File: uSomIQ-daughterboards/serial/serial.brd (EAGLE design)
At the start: 100 x 80 mm, 1 part

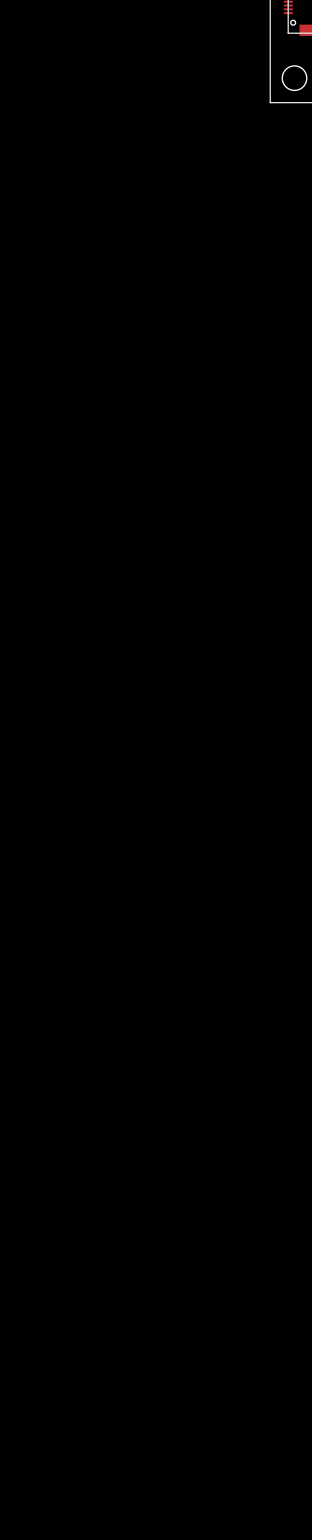
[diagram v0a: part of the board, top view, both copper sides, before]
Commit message: Add power supply and RTC
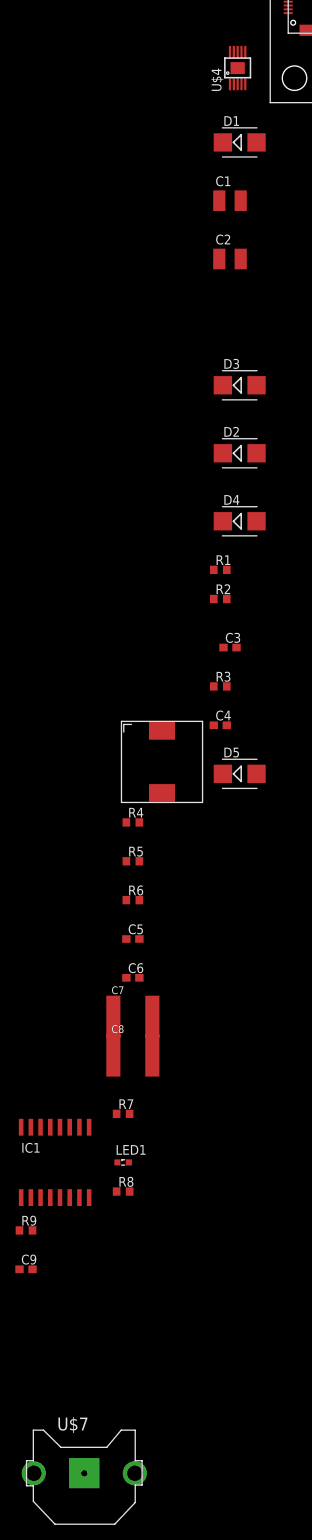
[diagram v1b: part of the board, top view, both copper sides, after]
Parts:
- added C1, C2: 4.7uF, 50V, rcl:C1210
- added C3: 0.01uF, 50V, rcl:C0603
- added C4: 0.1uF, 50V, rcl:C0603
- added C5: 5600pF, 25V, rcl:C0603
- added C6: 330pF, 50V, rcl:C0603
- added C7, C8: 47uF, 16V, rcl:C2220K
- added C9: 1uF, 16V, rcl:C0603
- added D1, D2, D5: B360B, diode:SMB
- added D3, D4: 47V, diode:SMB
- added IC1: DS3231/SO, adafruit:SO16W
- added L1: 27uH, 4.3A, power-supplies:7447798271
- added LED1: (no value), led:SML0603
- added R1: 384K, rcl:R0603
- added R2: 69.8K, rcl:R0603
- added R3: 412K, rcl:R0603
- added R4: 53.6K, rcl:R0603
- added R5, R7: 10K, rcl:R0603
- added R6: 11K, rcl:R0603
- added R8, R9: 100, rcl:R0603
- added U$4: TPS54260, power-supplies:S-PDSO-G10
- added U$7: (no value), adafruit:CR1220-THM
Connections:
- new net GND: C1.2, C2.2, C3.2, C5.2, C6.2, C7.2, C8.2, C9.2, D3.A, D4.A, D5.A, IC1.13, LED1.C, R2.1, R3.1, R5.1, U$3.MOUNT@0, U$3.MOUNT@1, U$3.MOUNT@2, U$3.MOUNT@3, U$4.9, U$4.PAD, U$7.-
- new net I2C0_SCL: IC1.16
- new net I2C0_SDA: IC1.15
- new net N$1: C1.1, C2.1, D1.C, D3.C, U$4.2
- new net N$10: C6.1, R6.2, U$4.8
- new net N$11: C5.1, R6.1
- new net N$12: IC1.14, U$7.+1
- new net N$2: C3.1, U$4.4
- new net N$3: D2.C, D4.C, R1.1
- new net N$4: R1.2, R2.2, U$4.3
- new net N$5: R3.2, U$4.5
- new net N$6: C4.1, U$4.1
- new net N$7: C4.2, D5.C, L1.P$1, U$4.10
- new net N$8: IC1.1, R9.2
- new net N$9: R4.1, R5.2, U$4.7
- new net RESET: R8.1
- new net RTC_32KHZ: R9.1
- new net VBATT: D1.A
- new net VDD: C7.1, C8.1, C9.1, IC1.2, L1.P$2, R4.2, R7.2
- new net VDD_PGOOD: LED1.A, R7.1, R8.2, U$4.6
- new net VIGN: D2.A

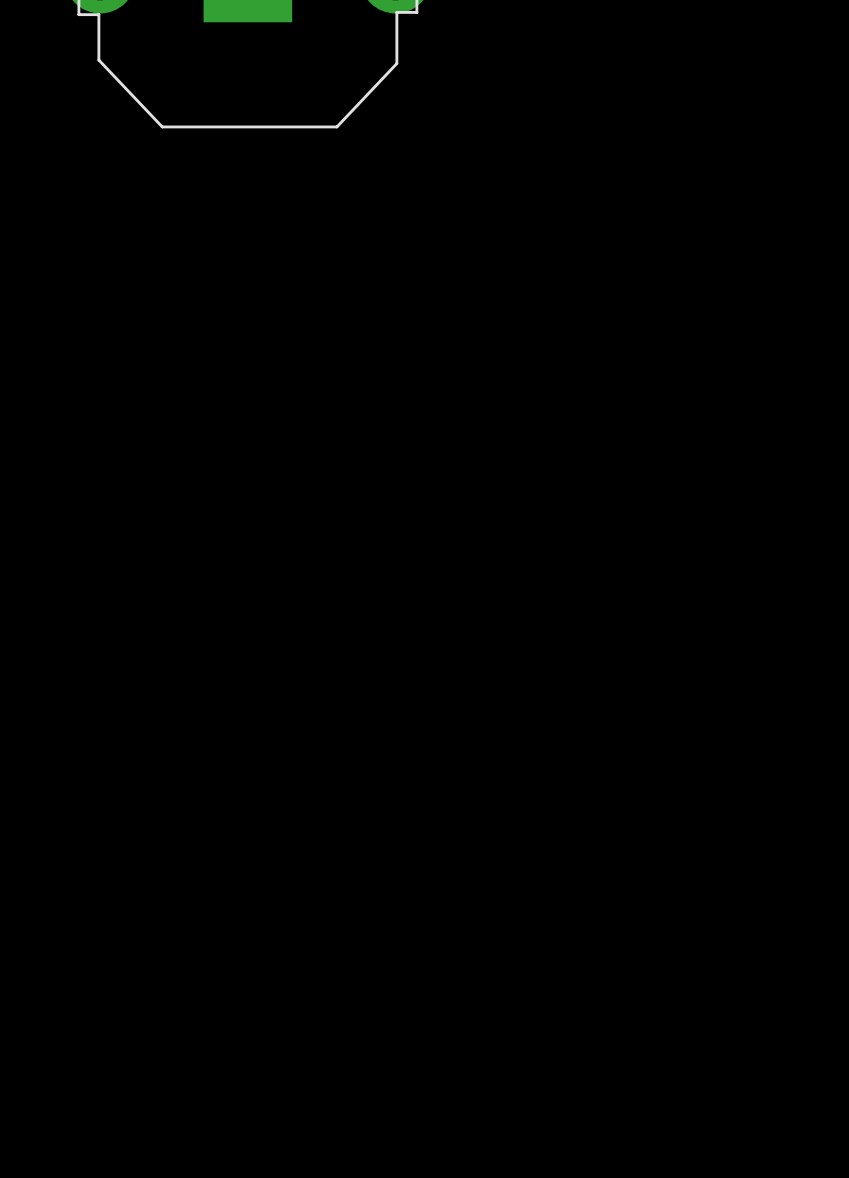
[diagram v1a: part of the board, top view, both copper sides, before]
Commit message: Add serial port connectors
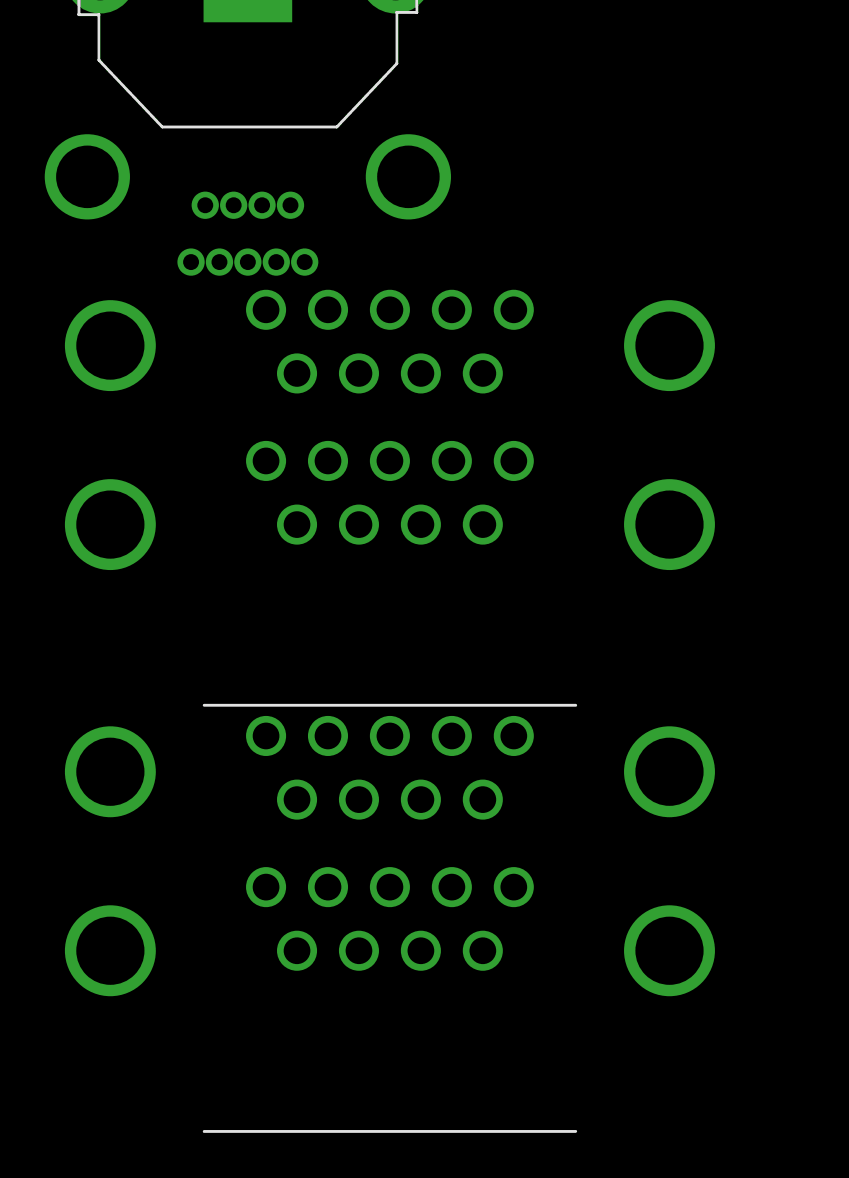
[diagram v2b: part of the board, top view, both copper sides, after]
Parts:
- added U$6: 83611-9006, connectors:83611-9006
- added U$8, U$9: 189-009-613R571, connectors:189-009-613R571
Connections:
- new net CAN_H: U$6.5
- new net CAN_L: U$6.6
- new net ETH_RX+: U$6.3
- new net ETH_RX-: U$6.4
- new net ETH_TX+: U$6.1
- new net ETH_TX-: U$6.2
- new net SP0-1PPS: U$8.A-1
- new net SP0-RX: U$8.A-2
- new net SP0-TX: U$8.A-3
- new net SP1-1PPS: U$8.B-1
- new net SP1-RX: U$8.B-3
- new net SP1-TX: U$8.B-4
- new net SP2-1PPS: U$9.A-1
- new net SP2-RX: U$9.A-2
- new net SP2-TX: U$9.A-3
- new net SP3-1PPS: U$9.B-1
- new net SP3-RX: U$9.B-3
- new net SP3-TX: U$9.B-4
- net GND: now also U$6.9, U$6.MOUNT@1, U$6.MOUNT@2, U$8.A-5, U$8.B2, U$8.MOUNT@1, U$8.MOUNT@2, U$8.MOUNT@3, U$8.MOUNT@4, U$9.A-5, U$9.B2, U$9.MOUNT@1, U$9.MOUNT@2, U$9.MOUNT@3, U$9.MOUNT@4
- net VBATT: now also U$6.7
- net VIGN: now also U$6.8
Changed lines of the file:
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@@
 <element name="C9" library="rcl" package="C0603" value="1uF, 16V" x="-100.33" y="-152.4"/>
 <element name="U$7" library="adafruit" package="CR1220-THM" value="" x="-92.71" y="-179.07"/>
+<element name="U$6" library="connectors" package="83611-9006" value="83611-9006" x="-95.25" y="-191.77"/>
+<element name="U$8" library="connectors" package="189-009-613R571" value="189-009-613R571" x="-86.36" y="-200.66"/>
+<element name="U$9" library="connectors" package="189-009-613R571" value="189-009-613R571" x="-86.36" y="-219.71"/>
 </elements>
 <signals>
 <signal name="VBATT">
 <contactref element="D1" pad="A"/>
+<contactref element="U$6" pad="7"/>
+<wire x1="-93.345" y1="-189.23" x2="-70.19" y2="-5.08" width="0" layer="19" extent="1-1"/>
 </signal>
 <signal name="N$1">
@@
 <contactref element="C9" pad="2"/>
 <contactref element="U$7" pad="-"/>
+<contactref element="U$6" pad="9"/>
+<contactref element="U$6" pad="MOUNT@1"/>
+<contactref element="U$6" pad="MOUNT@2"/>
+<contactref element="U$8" pad="MOUNT@1"/>
+<contactref element="U$8" pad="MOUNT@2"/>
+<contactref element="U$8" pad="MOUNT@3"/>
+<contactref element="U$8" pad="MOUNT@4"/>
+<contactref element="U$9" pad="MOUNT@1"/>
+<contactref element="U$9" pad="MOUNT@2"/>
+<contactref element="U$9" pad="MOUNT@3"/>
+<contactref element="U$9" pad="MOUNT@4"/>
+<contactref element="U$8" pad="A-5"/>
+<contactref element="U$8" pad="B2"/>
+<contactref element="U$9" pad="A-5"/>
+<contactref element="U$9" pad="B2"/>
 <wire x1="-88.38" y1="-138.43" x2="-99.48" y2="-152.4" width="0" layer="19" extent="1-1"/>
 <wire x1="-97.155" y1="-133.83" x2="-88.38" y2="-138.43" width="0" layer="19" extent="1-1"/>
@@
 <wire x1="-63.5" y1="31.0575" x2="-63.5" y2="9.5825" width="0" layer="19" extent="1-1"/>
 <wire x1="-92.71" y1="-179.07" x2="-99.48" y2="-152.4" width="0" layer="19" extent="1-1"/>
+<wire x1="-90.805" y1="-189.23" x2="-92.71" y2="-179.07" width="0" layer="19" extent="1-1"/>
+<wire x1="-89.1286" y1="-193.9036" x2="-90.805" y2="-189.23" width="0" layer="19" extent="1-1"/>
+<wire x1="-85.5345" y1="-187.96" x2="-90.805" y2="-189.23" width="0" layer="19" extent="1-1"/>
+<wire x1="-99.8855" y1="-187.96" x2="-90.805" y2="-189.23" width="0" layer="19" extent="1-1"/>
+<wire x1="-98.8568" y1="-195.5038" x2="-99.8855" y2="-187.96" width="0" layer="19" extent="1-1"/>
+<wire x1="-98.8568" y1="-203.5048" x2="-98.8568" y2="-195.5038" width="0" layer="19" extent="1-1"/>
+<wire x1="-80.8228" y1="-200.66" x2="-89.1286" y2="-193.9036" width="0" layer="19" extent="1-1"/>
+<wire x1="-73.8632" y1="-203.5048" x2="-80.8228" y2="-200.66" width="0" layer="19" extent="1-1"/>
+<wire x1="-73.8632" y1="-195.5038" x2="-73.8632" y2="-203.5048" width="0" layer="19" extent="1-1"/>
+<wire x1="-98.8568" y1="-214.5538" x2="-98.8568" y2="-203.5048" width="0" layer="19" extent="1-1"/>
+<wire x1="-98.8568" y1="-222.5548" x2="-98.8568" y2="-214.5538" width="0" layer="19" extent="1-1"/>
+<wire x1="-89.1286" y1="-212.9536" x2="-98.8568" y2="-214.5538" width="0" layer="19" extent="1-1"/>
+<wire x1="-80.8228" y1="-219.71" x2="-89.1286" y2="-212.9536" width="0" layer="19" extent="1-1"/>
+<wire x1="-73.8632" y1="-222.5548" x2="-80.8228" y2="-219.71" width="0" layer="19" extent="1-1"/>
+<wire x1="-73.8632" y1="-214.5538" x2="-73.8632" y2="-222.5548" width="0" layer="19" extent="1-1"/>
 <wire x1="-17.5" y1="31.0575" x2="-63.5" y2="31.0575" width="0" layer="19" extent="1-1"/>
 <wire x1="-17.5" y1="9.5825" x2="-17.5" y2="31.0575" width="0" layer="19" extent="1-1"/>
@@
 <signal name="VIGN">
 <contactref element="D2" pad="A"/>
+<contactref element="U$6" pad="8"/>
+<wire x1="-92.075" y1="-189.23" x2="-70.19" y2="-45.72" width="0" layer="19" extent="1-1"/>
 </signal>
 <signal name="N$3">
@@
 <wire x1="-99.314" y1="-179.07" x2="-98.425" y2="-133.83" width="0" layer="19" extent="1-1"/>
 </signal>
+<signal name="ETH_TX+">
+<contactref element="U$6" pad="1"/>
+</signal>
+<signal name="ETH_TX-">
+<contactref element="U$6" pad="2"/>
+</signal>
+<signal name="ETH_RX+">
+<contactref element="U$6" pad="3"/>
+</signal>
+<signal name="ETH_RX-">
+<contactref element="U$6" pad="4"/>
+</signal>
+<signal name="CAN_H">
+<contactref element="U$6" pad="5"/>
+</signal>
+<signal name="CAN_L">
+<contactref element="U$6" pad="6"/>
+</signal>
+<signal name="SP0-RX">
+<contactref element="U$8" pad="A-2"/>
+</signal>
+<signal name="SP0-TX">
+<contactref element="U$8" pad="A-3"/>
+</signal>
+<signal name="SP1-RX">
+<contactref element="U$8" pad="B-3"/>
+</signal>
+<signal name="SP1-TX">
+<contactref element="U$8" pad="B-4"/>
+</signal>
+<signal name="SP2-RX">
+<contactref element="U$9" pad="A-2"/>
+</signal>
+<signal name="SP2-TX">
+<contactref element="U$9" pad="A-3"/>
+</signal>
+<signal name="SP3-RX">
+<contactref element="U$9" pad="B-3"/>
+</signal>
+<signal name="SP3-TX">
+<contactref element="U$9" pad="B-4"/>
+</signal>
+<signal name="SP0-1PPS">
+<contactref element="U$8" pad="A-1"/>
+</signal>
+<signal name="SP1-1PPS">
+<contactref element="U$8" pad="B-1"/>
+</signal>
+<signal name="SP2-1PPS">
+<contactref element="U$9" pad="A-1"/>
+</signal>
+<signal name="SP3-1PPS">
+<contactref element="U$9" pad="B-1"/>
+</signal>
 </signals>

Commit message: Add RS232 transcievers
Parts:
- added C10, C11, C12, C13, C14, C17, C18, C19, C20, C21: 0.1uF, resistor:C0603
- added C15, C16, C22, C23: 10uF, resistor:C0603
- added R10, R11, R12, R13, R14, R15, R16, R17: 1k, resistor:R0603
- added TP1, TP2, TP3, TP4: TPB1,27, testpad:B1,27
- added U$10, U$11: ADM3311E, misc-ics:TSSOP28
- moved U$6 279.5 mm to (67.3, 35.6), turned to 270 degrees
- moved U$8 267.0 mm to (10.2, 48.3), turned to 270 degrees
- moved U$9 256.4 mm to (10.2, 17.8), turned to 270 degrees
- moved U$7 238.3 mm to (31.8, 24.1), turned to 270 degrees
- moved IC1 220.6 mm to (30.5, 41.9)
- moved L1 186.9 mm to (54.6, 36.8)
- moved U$3 105.9 mm to (41.9, 10.2), turned to 90 degrees
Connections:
- new net +3V3: C10.2, C15.1, C16.1, C17.2, C22.1, C23.1, R16.2, R17.2, U$10.3, U$11.3, U$3.P$6, U$3.P$8
- new net +5V: C7.1, C8.1, L1.P$2, R4.2, U$3.P$2, U$3.P$4
- new net N$13: C10.1, U$10.1
- new net N$14: C17.1, U$11.1
- new net N$15: C11.1, U$10.2
- new net N$16: C11.2, U$10.4
- new net N$17: R10.2, U$10.9
- new net N$18: TP1.TP, U$10.14
- new net N$19: TP2.TP, U$10.20
- new net N$20: R11.2, U$10.15
- new net N$21: R12.2, U$10.23
- new net N$22: C12.1, U$10.6
- new net N$23: C12.2, U$10.24
- new net N$24: C13.2, U$10.25
- new net N$25: C18.1, U$11.2
- new net N$26: C14.2, U$10.26
- new net N$27: C14.1, U$10.28
- new net N$28: C18.2, U$11.4
- new net N$29: R13.2, U$11.9
- new net N$30: TP3.TP, U$11.14
- new net N$31: TP4.TP, U$11.20
- new net N$32: R14.2, U$11.15
- new net N$33: R15.2, U$11.23
- new net N$34: C19.1, U$11.6
- new net N$35: C19.2, U$11.24
- new net N$36: C20.2, U$11.25
- new net N$37: C21.2, U$11.26
- new net N$38: C21.1, U$11.28
- new net N$40: R7.2
- new net SP0_1PPS: U$10.18, U$11.18
- new net SP0_RX: U$10.19, U$11.19
- new net SP0_TX: U$10.22, U$11.22
- new net SP1_1PPS: U$10.16, U$11.16
- new net SP1_RX: U$10.17, U$11.17
- new net SP1_TX: U$10.21, U$11.21
- new net UART0_1PPS: U$10.11, U$11.11, U$3.P$33
- new net UART0_RX: U$10.10, U$11.10, U$3.P$29
- new net UART0_TX: U$10.7, U$11.7, U$3.P$31
- new net UART1_1PPS: U$10.13, U$11.13, U$3.P$40
- new net UART1_RX: U$10.12, U$11.12, U$3.P$37
- new net UART1_TX: U$10.8, U$11.8, U$3.P$39
- new net UART2_1PPS: U$3.P$50
- new net UART2_RX: U$3.P$49
- new net UART2_TX: U$3.P$47
- new net UART3_1PPS: U$3.P$46
- new net UART3_RX: U$3.P$41
- new net UART3_TX: U$3.P$43
- new net XCVR_EN: R16.1, R17.1, U$10.5, U$11.5
- net GND: now also C13.1, C15.2, C16.2, C20.1, C22.2, C23.2, R10.1, R11.1, R12.1, R13.1, R14.1, R15.1, U$10.27, U$11.27, U$3.P$1, U$3.P$3
- net I2C0_SCL: now also U$3.P$12
- net I2C0_SDA: now also U$3.P$10
- net VDD: no longer C7.1, C8.1, L1.P$2, R4.2, R7.2

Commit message: Update libraries, add power supply monitoring
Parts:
- added C201: 0.1uF, rcl:C1210
- added C210, C211: 0.1uF, rcl:C0603
- added D202, D207: BAS40, diode:SOT23
- added D208, D209: 1.8V, diode:SMB
- added LED301, LED302: (no value), led:SML0603
- added R209, R210: 20K, rcl:R0603
- added R211, R212: 1K, rcl:R0603
- added R301, R302: 10K, rcl:R0603
- added R405: 100, rcl:R0603
- added X301: MINI-USB-UX60-MB-5ST, con-hirose:UX60-MB-5ST
- R201: value 100 -> NL
- renumbered C1 to C202, C10 to C403, C11 to C402, C12 to C405, C13 to C407, C14 to C408, C15 to C401, C16 to C404, C17 to C411, C18 to C410, C19 to C413, C2 to C203, C20 to C414, C21 to C415, C22 to C409, C23 to C412, C3 to C204, C4 to C205, C5 to C206, C6 to C207, C7 to C208, C8 to C209, C9 to C406, D1 to D201, D2 to D203, D3 to D204, D4 to D205, D5 to D206, IC1 to IC401, L1 to L201, LED1 to LED201, R1 to R203, R10 to R402, R11 to R403, R12 to R406, R13 to R408, R14 to R409, R15 to R410, R16 to R401, R17 to R407, R2 to R204, R3 to R205, R4 to R207, R5 to R208, R6 to R206, R7 to R202, R8 to R201, R9 to R404, U$10 to U401, U$11 to U402, U$3 to P301, U$4 to U201, U$6 to P102, U$7 to B401, U$8 to P101, U$9 to P103
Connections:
- removed net N$1: C202.1, C203.1, D201.C, D204.C, U201.2
- removed net SP0-1PPS: P101.A-1
- removed net SP0-RX: P101.A-2
- removed net SP0-TX: P101.A-3
- removed net SP1-1PPS: P101.B-1
- removed net SP1-RX: P101.B-3
- removed net SP1-TX: P101.B-4
- removed net SP2-1PPS: P103.A-1
- removed net SP2-RX: P103.A-2
- removed net SP2-TX: P103.A-3
- removed net SP3-1PPS: P103.B-1
- removed net SP3-RX: P103.B-3
- removed net SP3-TX: P103.B-4
- removed net VDD: C406.1, IC401.2
- new net ADC_VBATT: C211.1, D209.C, P301.P$13, R210.2, R212.2
- new net ADC_VIGN: C210.1, D208.C, P301.P$11, R209.2, R211.2
- new net LED_ETH_100MB: P301.P$67, R301.2
- new net LED_ETH_ACTIVE: P301.P$69, R302.2
- new net N$39: IC401.4, R405.2
- new net N$42: D207.3, R209.1
- new net PWR_EN: D202.1, P301.P$38
- new net RTC_RST: R405.1
- new net SP2_1PPS: P103.A-1, U402.18
- new net SP2_RX: P103.A-2, U402.19
- new net SP2_TX: P103.A-3, U402.22
- new net SP3_1PPS: P103.B-1, U402.16
- new net SP3_RX: P103.B-3, U402.17
- new net SP3_TX: P103.B-4, U402.21
- new net USB_D+: P301.P$61, X301.3
- new net USB_D-: P301.P$63, X301.2
- new net VBATT_PROTECTED: C201.1, C202.1, C203.1, D201.C, D204.C, R210.1, U201.2
- new net VDD_PGOOD1: LED301.A, R301.1
- new net VDD_PGOOD2: LED302.A, R302.1
- net +3V3: now also C406.1, IC401.2
- net ETH_RX+: now also P301.P$62
- net ETH_RX-: now also P301.P$64, P301.P$70
- net ETH_TX+: now also P301.P$68
- net GND: now also C201.2, C210.2, C211.2, D208.A, D209.A, LED301.C, LED302.C, P301.P$129, P301.P$135, P301.P$27, P301.P$59, P301.P$60, P301.P$65, P301.P$66, P301.P$9, P301.P$91, P301.P$92, R211.1, R212.1, X301.5
- net SP0_1PPS: now also P101.A-1; no longer U402.18
- net SP0_RX: now also P101.A-2; no longer U402.19
- net SP0_TX: now also P101.A-3; no longer U402.22
- net SP1_1PPS: now also P101.B-1; no longer U402.16
- net SP1_RX: now also P101.B-3; no longer U402.17
- net SP1_TX: now also P101.B-4; no longer U402.21
- net UART0_1PPS: no longer U402.11
- net UART0_RX: no longer U402.10
- net UART0_TX: no longer U402.7
- net UART1_1PPS: no longer U402.13
- net UART1_RX: no longer U402.12
- net UART1_TX: no longer U402.8
- net UART2_1PPS: now also U402.11
- net UART2_RX: now also U402.10
- net UART2_TX: now also U402.7
- net UART3_1PPS: now also U402.13
- net UART3_RX: now also U402.12
- net UART3_TX: now also U402.8
- net VIGN: now also D207.1

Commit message: Start to place serial daughterboard power supply
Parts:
- removed C203: 4.7uF, 50V, rcl:C1210
- removed C208: 47uF, 16V, rcl:C2220K
- removed D203: B360B, diode:SMB
- removed R201: NL, rcl:R0603
- added D1: BAS40, diode:SOT23
- added TP5, TP6: TPB1,27, testpad:B1,27
- D205: device diode:SMB -> diode:SOT23
- moved X301 424.6 mm to (57.1, 26.7), turned to 180 degrees
- moved LED302 418.6 mm to (59.7, 15.2), turned to 180 degrees
- moved LED301 411.6 mm to (59.7, 17.8), turned to 180 degrees
- moved D207 411.5 mm to (16.5, 76.2), turned to 270 degrees
- moved R302 411.3 mm to (54.6, 15.2), turned to 180 degrees
- moved R301 404.3 mm to (54.6, 17.8), turned to 180 degrees
- moved C201 395.6 mm to (27.9, 63.5), turned to 270 degrees
- moved D202 366.7 mm to (16.5, 72.4), turned to 270 degrees
- moved U402 282.3 mm to (29.2, 20.3), turned to 90 degrees
- moved LED201 251.3 mm to (34.3, 81.3), turned to 180 degrees
- moved C209 242.4 mm to (45.7, 78.7), turned to 180 degrees
- moved U401 236.8 mm to (29.2, 41.9), turned to 90 degrees
- moved C207 221.2 mm to (34.3, 71.1), turned to 270 degrees
- moved C206 215.6 mm to (31.8, 71.1), turned to 90 degrees
- moved R206 209.9 mm to (29.2, 71.1), turned to 90 degrees
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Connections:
- removed net N$40: R202.2
- removed net RESET: R201.1
- removed net RTC_32KHZ: R404.1
- removed net RTC_RST: R405.1
- new net N$1: R404.1, TP5.TP
- new net N$41: R405.1, TP6.TP
- net +5V: now also R202.2; no longer C208.1
- net ETH_RX-: no longer P301.P$70
- net ETH_TX-: now also P301.P$70
- net GND: now also D205.1; no longer C203.2, C208.2, D205.A
- net N$3: now also D1.3, D205.3; no longer D203.C, D205.C
- net N$4: now also D202.3
- net VBATT_PROTECTED: no longer C203.1
- net VDD_PGOOD: no longer R201.2
- net VIGN: now also D1.1; no longer D203.A
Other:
- board size 100 x 80 mm -> 63.2 x 83.8 mm

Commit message: Initial part placement for serial daughterboard
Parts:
- removed C401, C409: 10uF, resistor:C0603
- removed R404, R405: 100, rcl:R0603
- D208, D209: device diode:SMB -> diode:SOT23
- moved C211 439.2 mm to (53.3, 61.0), turned to 180 degrees
- moved R212 436.9 mm to (53.3, 63.5)
- moved D209 429.5 mm to (48.3, 64.8)
- moved R210 427.4 mm to (53.3, 66.0)
- moved D208 421.2 mm to (58.4, 64.8)
- moved TP6 411.4 mm to (41.9, 24.1)
- moved TP5 405.4 mm to (38.1, 24.1)
- moved R211 395.7 mm to (44.5, 63.5), turned to 180 degrees
- moved C210 381.6 mm to (44.5, 61.0)
- moved R209 381.6 mm to (44.5, 66.0)
- moved R401 331.4 mm to (35.6, 43.2), turned to 90 degrees
- moved R407 318.7 mm to (35.6, 24.1), turned to 270 degrees
- moved R408 308.4 mm to (35.6, 27.9), turned to 270 degrees
- moved TP4 307.3 mm to (40.6, 17.8)
- moved R409 303.3 mm to (22.9, 30.5), turned to 270 degrees
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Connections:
- removed net N$1: R404.1, TP5.TP
- removed net N$41: R405.1, TP6.TP
- net +3V3: no longer C401.1, C409.1
- net ADC_VBATT: now also D209.3; no longer D209.C
- net ADC_VIGN: now also D208.3; no longer D208.C
- net GND: now also D208.1, D209.1; no longer C401.2, C409.2, D208.A, D209.A
- net N$39: now also TP6.TP; no longer R405.2
- net N$8: now also TP5.TP; no longer R404.2
